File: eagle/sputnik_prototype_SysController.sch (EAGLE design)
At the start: 45 parts, among them U1 MEGA128-M, U2 MIC5219 3.3V, Y2 8MHZ

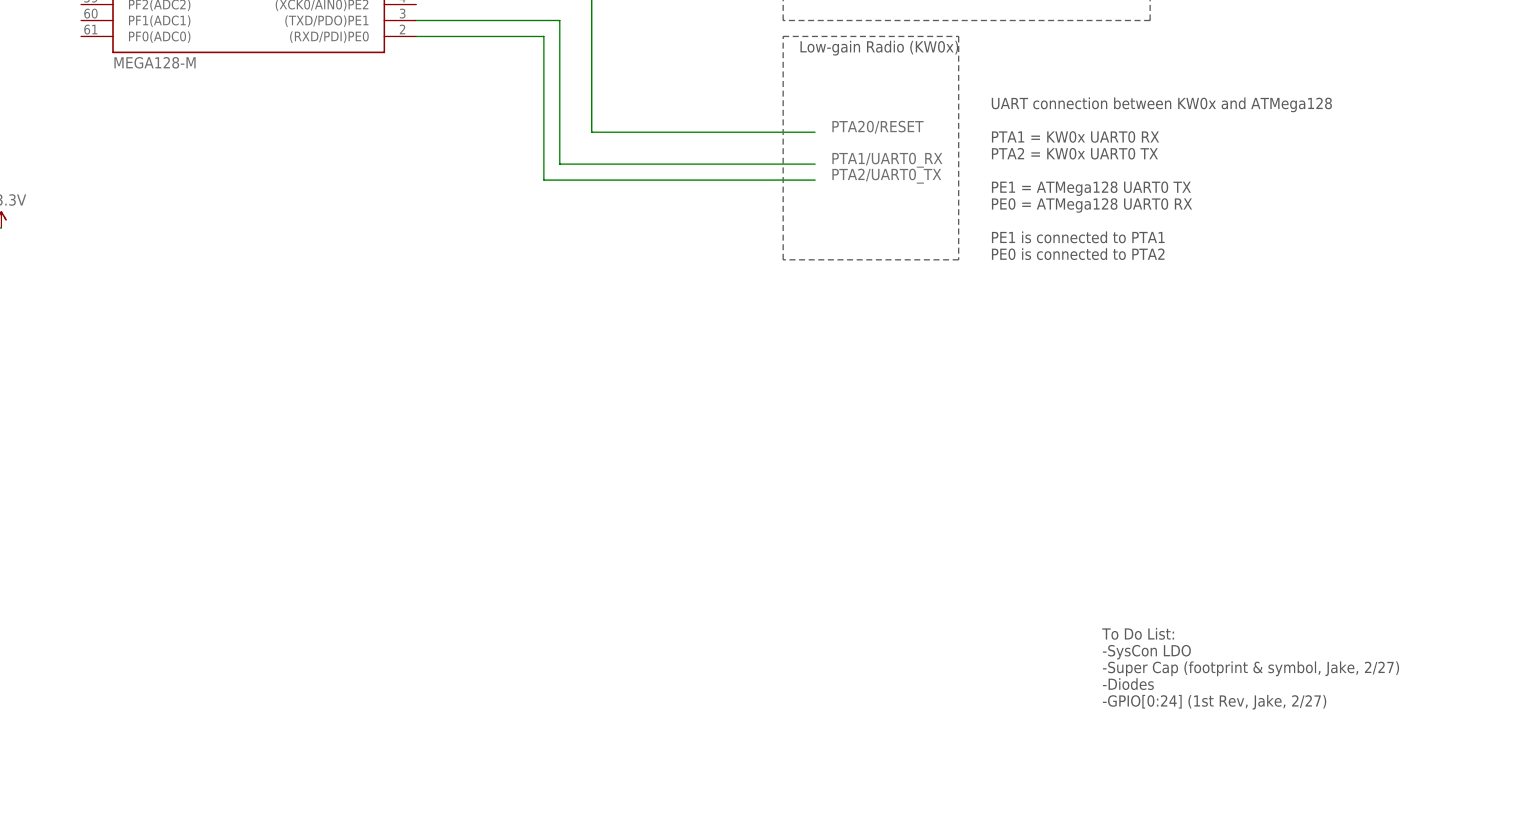
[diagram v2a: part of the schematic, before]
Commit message: Added LNA LDO footprint and circuitry
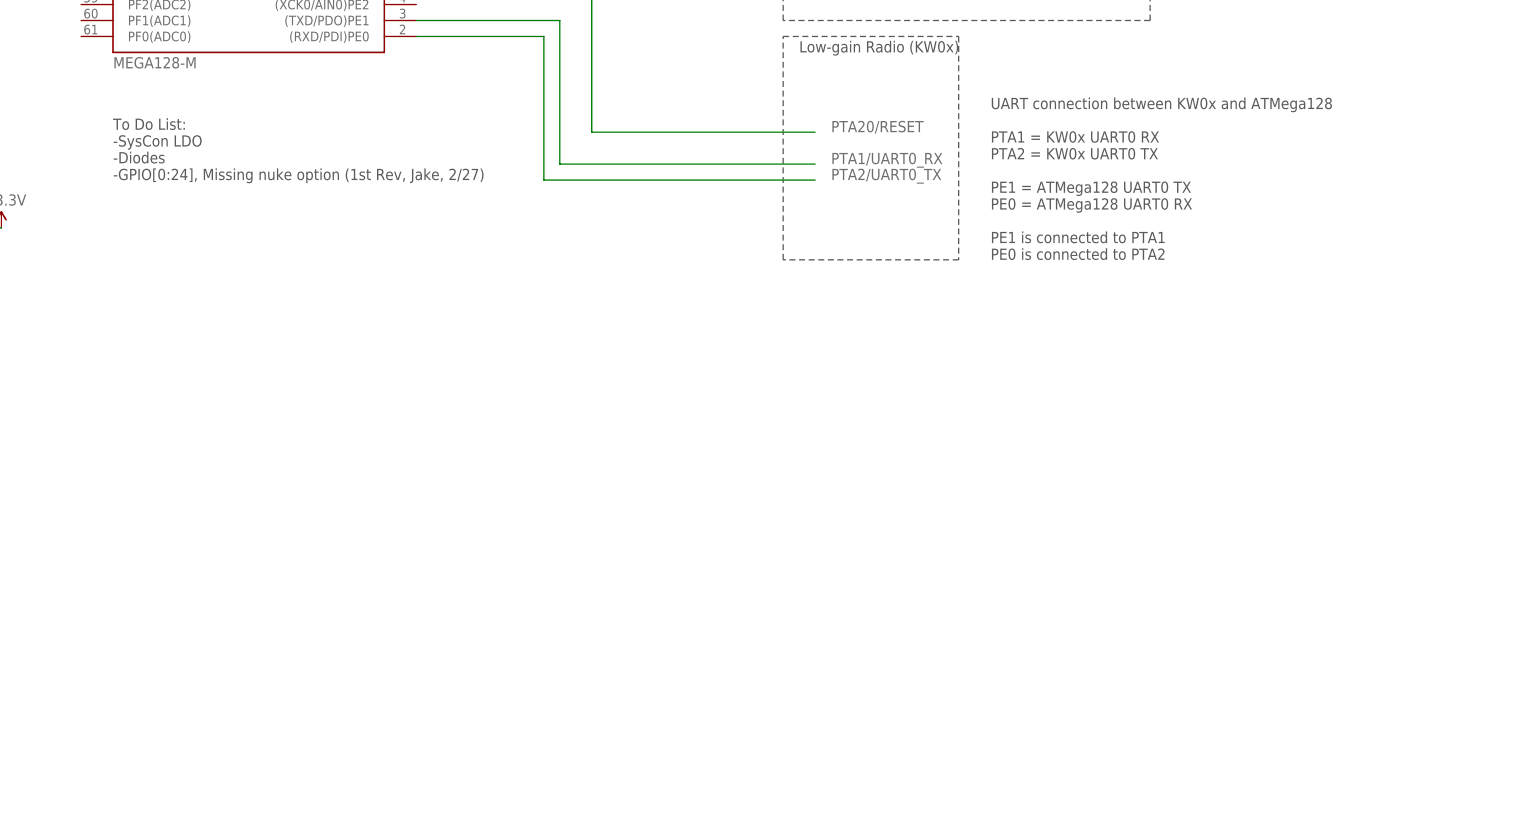
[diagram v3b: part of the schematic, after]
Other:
- note added: "To Do List: -SysCon LDO -Diodes -GPIO[0:24], Missing nuke option (1st Rev, Jake, 2/27)"
- note removed: "To Do List: -SysCon LDO -Super Cap (footprint & symbol, Jake, 2/27) -Diodes -GPIO[0:24] (1st Rev, Jake, 2/27)"
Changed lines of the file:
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@@
 <wire x1="393.7" y1="124.46" x2="393.7" y2="160.02" width="0.1524" layer="97" style="longdash"/>
 <text x="396.24" y="157.48" size="1.778" layer="97">Low-gain Radio (KW0x)</text>
-<text x="444.5" y="53.34" size="1.778" layer="97">To Do List:
+<text x="287.02" y="137.16" size="1.778" layer="97">To Do List:
 -SysCon LDO
--Super Cap (footprint &amp; symbol, Jake, 2/27)
 -Diodes
--GPIO[0:24] (1st Rev, Jake, 2/27)</text>
+-GPIO[0:24], Missing nuke option (1st Rev, Jake, 2/27)</text>
 <text x="431.8" y="287.02" size="1.778" layer="97">GPIO</text>
 <text x="431.8" y="248.92" size="1.778" layer="97">GPIO</text>

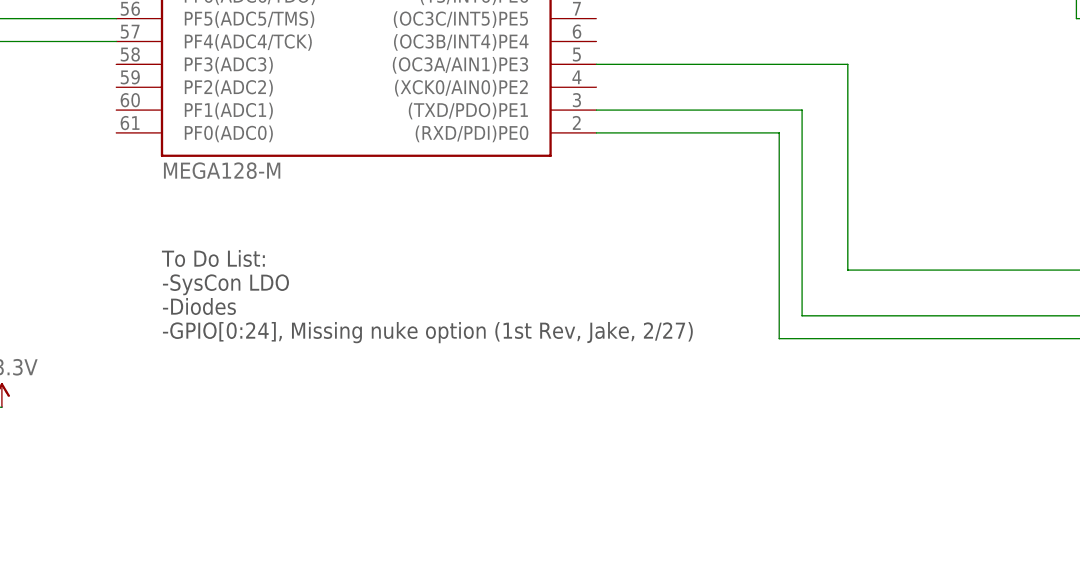
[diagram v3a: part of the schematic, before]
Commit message: Updated to do list
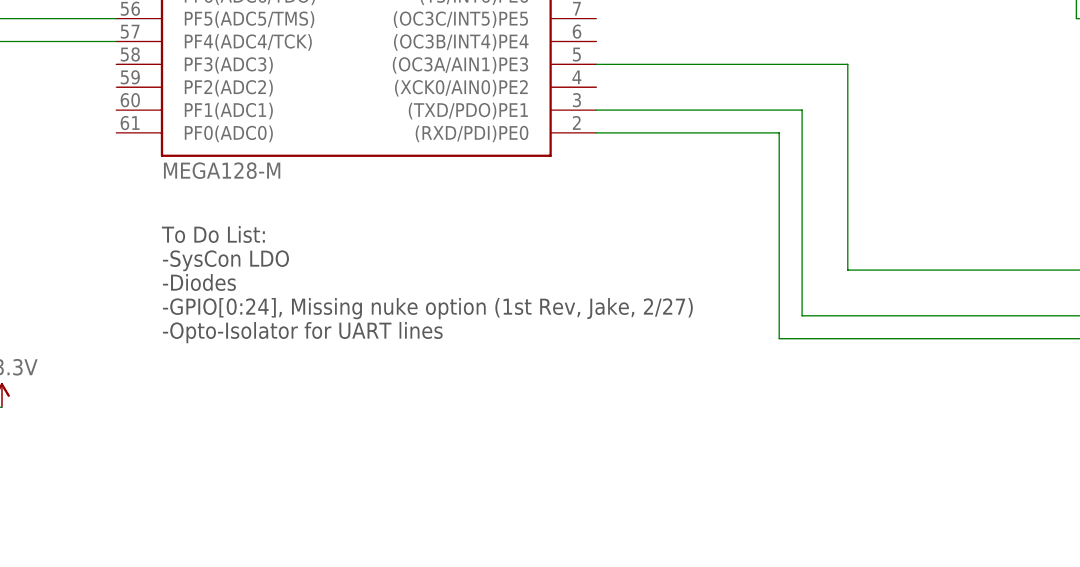
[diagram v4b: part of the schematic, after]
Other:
- note added: "To Do List: -SysCon LDO -Diodes -GPIO[0:24], Missing nuke option (1st Rev, Jake, 2/27) -Opto-Isolator for UART lines"
- note removed: "To Do List: -SysCon LDO -Diodes -GPIO[0:24], Missing nuke option (1st Rev, Jake, 2/27)"
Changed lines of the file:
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@@
 -SysCon LDO
 -Diodes
--GPIO[0:24], Missing nuke option (1st Rev, Jake, 2/27)</text>
+-GPIO[0:24], Missing nuke option (1st Rev, Jake, 2/27)
+-Opto-Isolator for UART lines</text>
 <text x="431.8" y="287.02" size="1.778" layer="97">GPIO</text>
 <text x="431.8" y="248.92" size="1.778" layer="97">GPIO</text>

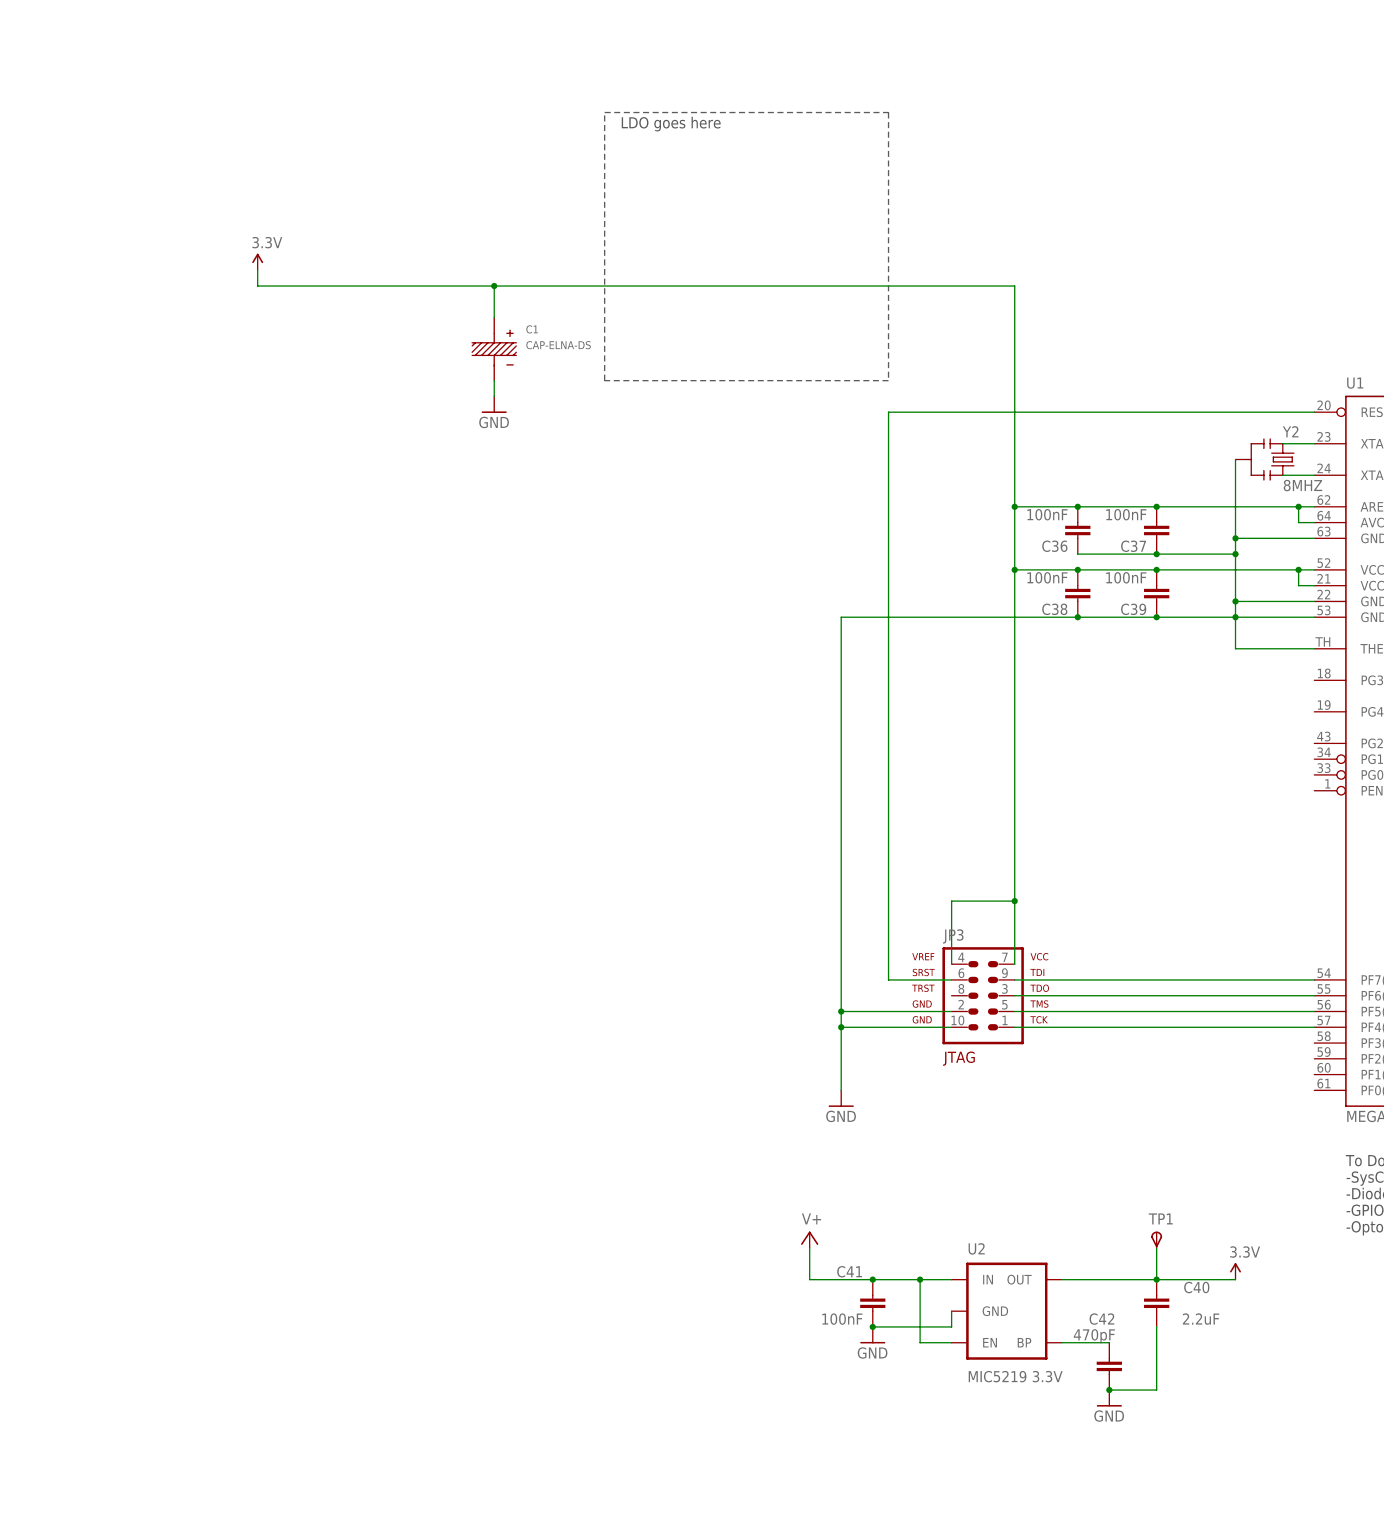
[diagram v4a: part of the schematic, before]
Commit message: Added rad-hard model LDO
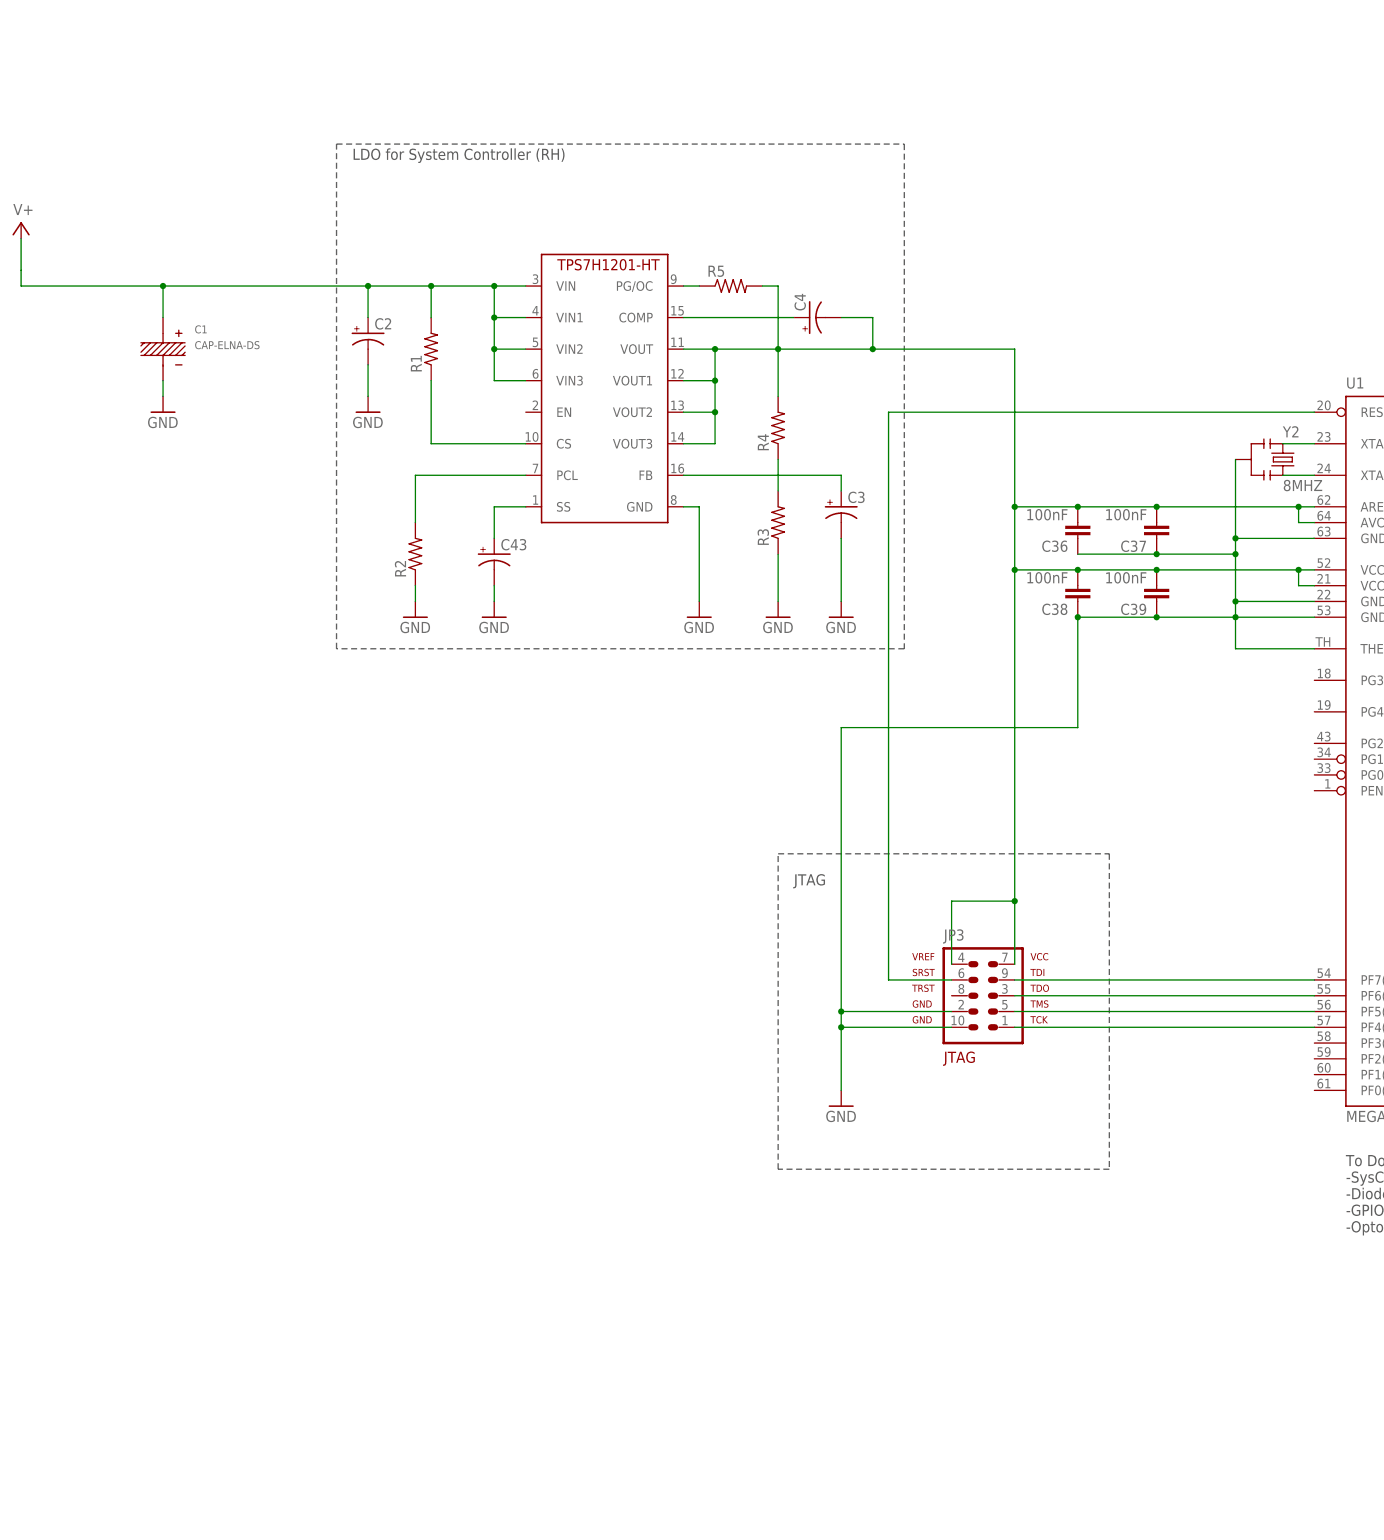
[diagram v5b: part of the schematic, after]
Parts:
- removed C40: 2.2uF, rcl_custom:C-EU0603-B-NOSILK
- removed C41: 100nF, rcl_custom:C-EU0603-B-NOSILK
- removed C42: 470pF, rcl_custom:C-EU0603-B-NOSILK
- removed TP1: TPSPAD1-13, testpad:TPSPAD1-13
- removed U2: MIC5219 3.3V, Lilypad_Arduino_USB_v12:SPARKFUN-POWERIC_V_REG_MIC52193.3V
- added C2, C3, C4, C43: (no value), rcl:CPOL-USCT6032
- added R1, R2, R3, R4, R5: (no value), rcl_custom:R-US_0603-B-NOSILK
- added U$1: TPS7H1201-HT, psas_c3_team05:TPS7H1201-HT
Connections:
- removed net 3.3V: C1.+, C36.2, C37.2, C38.2, C39.2, C40.2, JP3.4, JP3.7, TP1.PP, U1.AREF, U1.AVCC, U1.VCC, U1.VCC@1, U2.OUT
- new net N$1: C36.2, C37.2, C38.2, C39.2, C4.-, JP3.4, JP3.7, R4.2, R5.2, U$1.VOUT, U$1.VOUT1, U$1.VOUT2, U$1.VOUT3, U1.AREF, U1.AVCC, U1.VCC, U1.VCC@1
- new net N$2: C43.+, U$1.SS
- new net N$4: C3.+, U$1.FB
- new net N$5: C4.+, U$1.COMP
- new net N$6: R3.2, R4.1
- new net N$7: R5.1, U$1.PG/OC
- new net N$8: R2.2, U$1.PCL
- new net N$9: R1.1, U$1.CS
- net GND: now also C2.-, C3.-, C43.-, R2.1, R3.1, U$1.GND; no longer C40.1, C41.1, C42.1, U2.GND
- net N$3: now also C1.+, C2.+, R1.2, U$1.VIN, U$1.VIN1, U$1.VIN2, U$1.VIN3; no longer C42.2, U2.BP
- net V+: no longer C41.2, U2.EN, U2.IN
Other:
- note added: "JTAG"
- note added: "LDO for System Controller (RH)"
- note removed: "LDO goes here"
- moved on the sheet: C1

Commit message: Fixed to do list
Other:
- note added: "To Do List: -Diodes -GPIO[0:24], Missing nuke option (1st Rev, Jake, 2/27) -Opto-Isolator for UART lines"
- note removed: "To Do List: -SysCon LDO -Diodes -GPIO[0:24], Missing nuke option (1st Rev, Jake, 2/27) -Opto-Isolator for UART lines"
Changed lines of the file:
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@@
 <text x="396.24" y="157.48" size="1.778" layer="97">Low-gain Radio (KW0x)</text>
 <text x="287.02" y="137.16" size="1.778" layer="97">To Do List:
--SysCon LDO
 -Diodes
 -GPIO[0:24], Missing nuke option (1st Rev, Jake, 2/27)
